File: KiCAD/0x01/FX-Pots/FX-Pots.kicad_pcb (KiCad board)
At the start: 2 copper layers, 50 x 100 mm, 28 parts, among them J1 Conn_01x05, J2 Conn_01x05, SW1 SW_Push_LED, SW2 SW_Push_LED, SW3 SW_Push_LED, SW4 SW_Push_LED, U1 74HC595, U2 CD74HC4067M

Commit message: fx-pots
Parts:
- removed C3: 1uF, Capacitor_SMD:C_1206_3216Metric_Pad1.33x1.80mm_HandSolder
- added C10: 1uF, Capacitor_SMD:C_1206_3216Metric_Pad1.33x1.80mm_HandSolder, F.Cu at (173.7, 105.3)
- added C11: 1uF, Capacitor_SMD:C_1206_3216Metric_Pad1.33x1.80mm_HandSolder, F.Cu at (174.2, 131.7)
- added C5: 1uF, Capacitor_SMD:C_1206_3216Metric_Pad1.33x1.80mm_HandSolder, F.Cu at (86.3, 75.7)
- added C6: 1uF, Capacitor_SMD:C_1206_3216Metric_Pad1.33x1.80mm_HandSolder, F.Cu at (86.1, 104.7)
- added C7: 1uF, Capacitor_SMD:C_1206_3216Metric_Pad1.33x1.80mm_HandSolder, F.Cu at (86.4, 131.5)
- added C8: 1uF, Capacitor_SMD:C_1206_3216Metric_Pad1.33x1.80mm_HandSolder, F.Cu at (174.0, 46.4)
- added C9: 1uF, Capacitor_SMD:C_1206_3216Metric_Pad1.33x1.80mm_HandSolder, F.Cu at (174.2, 76.2)
- added JP1: A0, Jumper:SolderJumper-2_P1.3mm_Open_RoundedPad1.0x1.5mm, B.Cu at (124.2, 90.6)
- added JP2: A1, Jumper:SolderJumper-2_P1.3mm_Open_RoundedPad1.0x1.5mm, B.Cu at (127.8, 90.6)
- added JP3: A0, Jumper:SolderJumper-2_P1.3mm_Open_RoundedPad1.0x1.5mm, B.Cu at (131.3, 90.6)
- added JP4: A1, Jumper:SolderJumper-2_P1.3mm_Open_RoundedPad1.0x1.5mm, B.Cu at (134.9, 90.6)
- added R10: 10K, PCM_Resistor_SMD_AKL:R_1206_3216Metric_Pad1.30x1.75mm_HandSolder, B.Cu at (100.4, 132.4)
- added R11: 220, PCM_Resistor_SMD_AKL:R_1206_3216Metric_Pad1.30x1.75mm_HandSolder, F.Cu at (160.5, 44.2)
- added R12: 220, PCM_Resistor_SMD_AKL:R_1206_3216Metric_Pad1.30x1.75mm_HandSolder, F.Cu at (165.4, 68.1)
- added R13: 220, PCM_Resistor_SMD_AKL:R_1206_3216Metric_Pad1.30x1.75mm_HandSolder, F.Cu at (165.2, 97.7)
- added R14: 220, PCM_Resistor_SMD_AKL:R_1206_3216Metric_Pad1.30x1.75mm_HandSolder, F.Cu at (165.4, 125.2)
- added R15: 10K, PCM_Resistor_SMD_AKL:R_1206_3216Metric_Pad1.30x1.75mm_HandSolder, B.Cu at (174.3, 50.3)
- added R16: 10K, PCM_Resistor_SMD_AKL:R_1206_3216Metric_Pad1.30x1.75mm_HandSolder, B.Cu at (174.1, 79.4)
- added R17: 10K, PCM_Resistor_SMD_AKL:R_1206_3216Metric_Pad1.30x1.75mm_HandSolder, B.Cu at (173.7, 108.5)
- added R18: 10K, PCM_Resistor_SMD_AKL:R_1206_3216Metric_Pad1.30x1.75mm_HandSolder, B.Cu at (174.2, 131.8)
- added R9: 10K, PCM_Resistor_SMD_AKL:R_1206_3216Metric_Pad1.30x1.75mm_HandSolder, F.Cu at (90.4, 112.3)
- added RN1: R_Pack04_10K, Resistor_SMD:R_Array_Convex_4x0603, F.Cu at (129.6, 96.6)
- added RV5: R_Pot, led-switch:Potentiometer_Bourns_PTV09A-1_Single_Vertical, F.Cu at (144.5, 53.6)
- added RV6: R_Pot, led-switch:Potentiometer_Bourns_PTV09A-1_Single_Vertical, F.Cu at (144.6, 82.7)
- added RV7: R_Pot, led-switch:Potentiometer_Bourns_PTV09A-1_Single_Vertical, F.Cu at (144.6, 111.7)
- added RV8: R_Pot, led-switch:Potentiometer_Bourns_PTV09A-1_Single_Vertical, F.Cu at (144.8, 138.2)
- added SW5: SW_Push_LED, led-switch:SW_PUSH_6mm_LED, F.Cu at (167.2, 46.4)
- added SW6: SW_Push_LED, led-switch:SW_PUSH_6mm_LED, F.Cu at (167.5, 75.5)
- added SW7: SW_Push_LED, led-switch:SW_PUSH_6mm_LED, F.Cu at (167.0, 104.6)
- added SW8: SW_Push_LED, led-switch:SW_PUSH_6mm_LED, F.Cu at (167.3, 131.2)
- C1, C2: value 1uF -> 10uF; footprint Capacitor_SMD:C_1206_3216Metric_Pad1.33x1.80mm_HandSolder -> Capacitor_SMD:C_0805_2012Metric_Pad1.18x1.45mm_HandSolder
- C4: moved to F.Cu
- J1: value Conn_01x05 -> IN; footprint Connector_PinSocket_2.54mm:PinSocket_1x05_P2.54mm_Vertical -> Connector_JST:JST_PH_S4B-PH-K_1x04_P2.00mm_Horizontal; moved to B.Cu
- J2: value Conn_01x05 -> OUT; footprint Connector_PinSocket_2.54mm:PinSocket_1x05_P2.54mm_Vertical -> Connector_JST:JST_PH_S4B-PH-K_1x04_P2.00mm_Horizontal; moved to B.Cu
- R1, R2: value 220 -> 10K; footprint PCM_Resistor_SMD_AKL:R_1206_3216Metric_Pad1.30x1.75mm_HandSolder -> Capacitor_SMD:C_0805_2012Metric_Pad1.18x1.45mm_HandSolder
- R5, R6: value 10K -> 220
- RV1, RV2, RV3, RV4: footprint Potentiometer_THT:Potentiometer_Bourns_PTV09A-1_Single_Vertical -> led-switch:Potentiometer_Bourns_PTV09A-1_Single_Vertical
- U1: value 74HC595 -> ADS7830; footprint Package_SO:SOIC-16_3.9x9.9mm_P1.27mm -> Package_SO:TSSOP-16_4.4x5mm_P0.65mm; moved to F.Cu
- U2: value CD74HC4067M -> ADS7830; footprint Package_SO:SOIC-24W_7.5x15.4mm_P1.27mm -> Package_SO:TSSOP-16_4.4x5mm_P0.65mm; moved to F.Cu
- moved C4 93.4 mm to (99.9, 46.8)
- moved J2 86.2 mm to (159.3, 115.5), turned to 180 degrees
- moved C2 78.7 mm to (152.6, 84.2)
- moved R3 65.1 mm to (99.9, 43.6)
- moved J1 63.8 mm to (102.4, 63.0), turned to 0 degrees
- moved R8 63.5 mm to (87.4, 69.1)
- moved R7 62.5 mm to (88.3, 52.7)
- moved H2 62.2 mm to (170.0, 60.7)
- moved H3 62.2 mm to (170.0, 119.6)
- moved U2 49.2 mm to (154.9, 90.7), turned to 90 degrees
- moved C1 44.0 mm to (104.0, 83.7)
- moved R5 41.1 mm to (91.4, 97.8), turned to 0 degrees
- moved R1 27.0 mm to (108.6, 67.3), turned to 90 degrees
- moved U1 25.4 mm to (106.3, 90.8), turned to 90 degrees
- moved R2 24.2 mm to (106.4, 67.3), turned to 90 degrees
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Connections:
- C1 pad 1: FXSW1 -> +5V
- C2 pad 1: FXSW2 -> +5V
- C4 pad 1: FXSW4 -> /FXSW1
- J1 pad 1: MPLEX-S0 -> GND
- J1 pad 2: MPLEX-S1 -> +5V
- J1 pad 3: MPLEX-AP -> /SDA
- J1 pad 4: MPLEX-S2 -> /SCL
- J2 pad 1: GND -> /SCL
- J2 pad 2: +5V -> /SDA
- J2 pad 3: SRCLK -> +5V
- J2 pad 4: FX-LED-LATCH -> GND
- R1 pad 1: GND -> +5V
- R1 pad 2: Net-(SW1-K) -> /SDA
- R2 pad 1: GND -> +5V
- R2 pad 2: Net-(SW2-K) -> /SCL
- R3 pad 2: Net-(SW3-K) -> Net-(SW1-K)
- R4 pad 2: Net-(SW4-K) -> Net-(SW2-K)
- R5 pad 1: +5V -> GND
- R5 pad 2: FXSW1 -> Net-(SW3-K)
- R6 pad 1: +5V -> GND
- R6 pad 2: FXSW2 -> Net-(SW4-K)
- R7 pad 2: FXSW3 -> /FXSW1
- R8 pad 2: FXSW4 -> /FXSW2
- RV1 pad 2: POT1 -> /POT1
- RV2 pad 2: POT2 -> /POT2
- RV3 pad 2: POT3 -> /POT3
- RV4 pad 2: POT4 -> /POT4
- SW1 pad 2: FXSW1 -> /FXSW1
- SW1 pad 4: FX-LED-1 -> /FX-LED-1
- SW2 pad 2: FXSW2 -> /FXSW2
- SW2 pad 4: FX-LED-2 -> /FX-LED-2
- SW3 pad 2: FXSW3 -> /FXSW3
- SW3 pad 4: FX-LED-3 -> /FX-LED-3
- SW4 pad 2: FXSW4 -> /FXSW4
- SW4 pad 4: FX-LED-4 -> /FX-LED-4
- U1 pad 1: unconnected-(U1-QB-Pad1) -> /POT1
- U1 pad 10: +5V -> unconnected-(U1-REFin/REFout-Pad10)
- U1 pad 11: SRCLK -> unconnected-(U1-COM-Pad11)
- U1 pad 12: FX-LED-LATCH -> /A0
- U1 pad 13: GND -> /A1
- U1 pad 14: FX-LED-SIG -> /SCL
- U1 pad 15: unconnected-(U1-QA-Pad15) -> /SDA
- U1 pad 2: FX-LED-1 -> /FXSW1
- U1 pad 3: FX-LED-2 -> /POT2
- U1 pad 4: FX-LED-3 -> /FXSW2
- U1 pad 5: FX-LED-4 -> /POT3
- U1 pad 6: unconnected-(U1-QG-Pad6) -> /FXSW3
- U1 pad 7: unconnected-(U1-QH-Pad7) -> /POT4
- U1 pad 8: GND -> /FXSW4
- U1 pad 9: unconnected-(U1-QH'-Pad9) -> GND
- U2 pad 1: MPLEX-AP -> /POT5
- U2 pad 10: MPLEX-S0 -> unconnected-(U2-REFin/REFout-Pad10)
- U2 pad 11: MPLEX-S1 -> unconnected-(U2-COM-Pad11)
- U2 pad 12: GND -> /A3
- U2 pad 13: MPLEX-S3 -> /A4
- U2 pad 14: MPLEX-S2 -> /SCL
- U2 pad 15: GND -> /SDA
- U2 pad 16: unconnected-(U2-I15-Pad16) -> +5V
- U2 pad 2: unconnected-(U2-I7-Pad2) -> /FXSW5
- U2 pad 3: unconnected-(U2-I6-Pad3) -> /POT6
- U2 pad 4: unconnected-(U2-I5-Pad4) -> /FXSW6
- U2 pad 5: FXSW2 -> /POT7
- U2 pad 6: FXSW1 -> /FXSW7
- U2 pad 7: POT1 -> /POT8
- U2 pad 8: POT2 -> /FXSW8
- U2 pad 9: unconnected-(U2-I0-Pad9) -> GND
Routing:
- added copper zone on B.Cu, net +5V
- added copper zone on F.Cu, net +5V
- added copper zone on F.Cu, net GND
- removed copper zone on B.Cu, net GND
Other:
- board size 50 x 100 mm -> 100.1 x 100 mm

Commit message: pads_demo
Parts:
- moved R1 2.18 mm to (106.4, 67.3)
- moved R2 2.18 mm to (108.6, 67.3)
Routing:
- net /SCL: track 0.00 -> 141.3 mm, vias 0 -> 10
- net /SDA: track 0.00 -> 130.3 mm, vias 0 -> 9
- net GND: track 0.00 -> 99.5 mm, vias 0 -> 1
- net /FXSW5: track 0.00 -> 77.8 mm, vias 0 -> 4
- net /POT8: track 0.00 -> 51.5 mm, vias 0 -> 2
- net /POT5: track 0.00 -> 48.1 mm, vias 0 -> 2
- net /FXSW6: track 0.00 -> 31.6 mm
- net /POT7: track 0.00 -> 30.2 mm
- net /A3: track 0.00 -> 27.5 mm, vias 0 -> 1
- net /A1: track 0.00 -> 26.8 mm, vias 0 -> 1
- net /POT6: track 0.00 -> 22.7 mm, vias 0 -> 1
- net /FXSW7: track 0.00 -> 21.3 mm, vias 0 -> 2
- net /A4: track 0.00 -> 21.0 mm, vias 0 -> 1
- net /A0: track 0.00 -> 18.8 mm, vias 0 -> 1
- net +5V: track 0.00 -> 16.7 mm, vias 0 -> 2
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
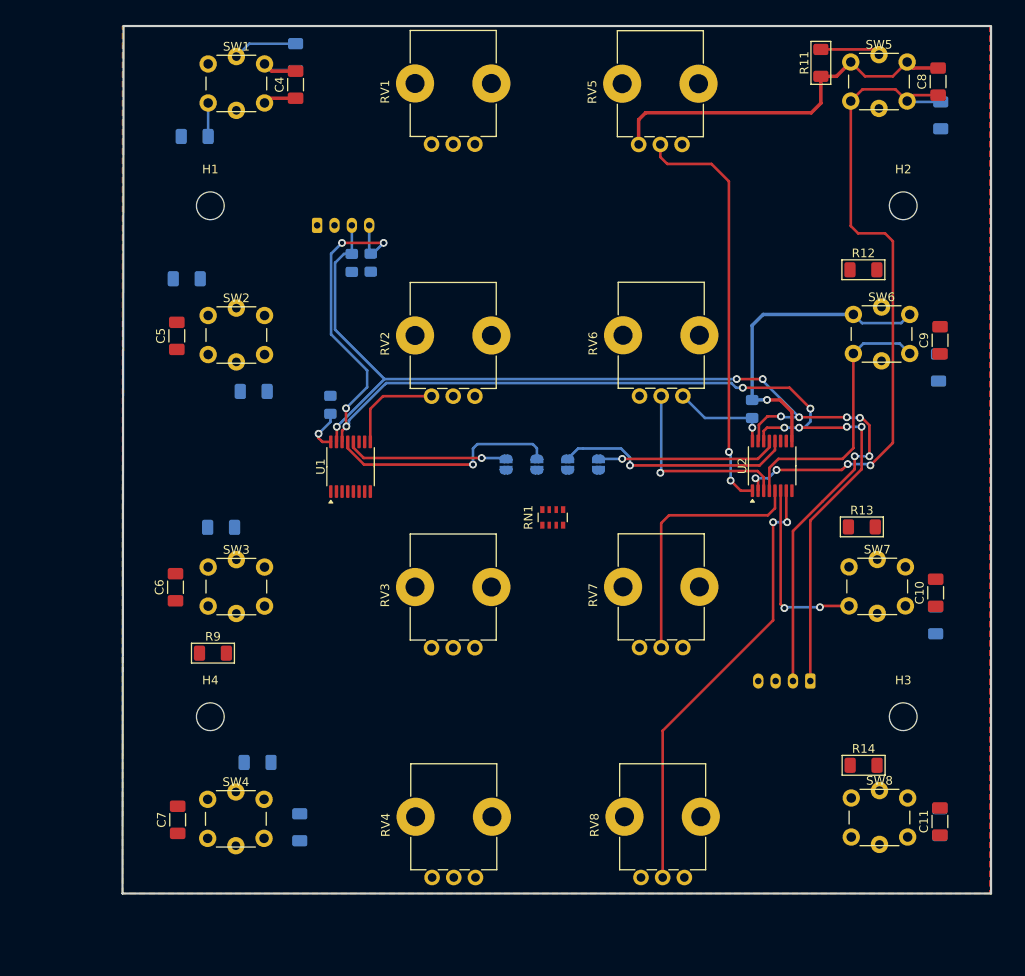
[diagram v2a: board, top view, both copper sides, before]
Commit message: fx pots routing
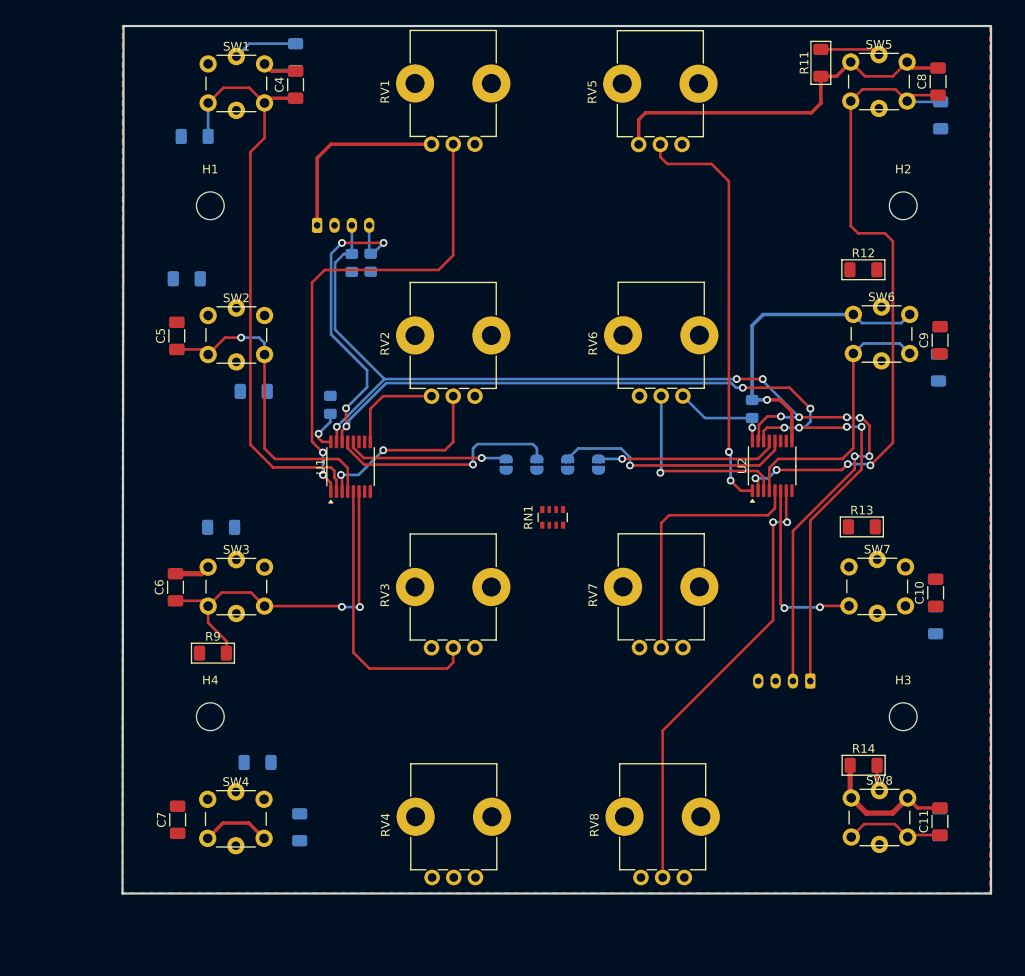
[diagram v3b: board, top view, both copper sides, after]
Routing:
- net /FXSW1: track 7.67 -> 69.1 mm
- net /POT1: track 0.00 -> 55.4 mm, vias 0 -> 2
- net /FXSW3: track 0.00 -> 42.5 mm, vias 0 -> 2
- net GND: track 99.5 -> 141.2 mm
- net /FXSW2: track 0.00 -> 36.8 mm, vias 0 -> 1
- net /POT3: track 0.00 -> 32.8 mm
- net /POT2: track 0.00 -> 21.8 mm, vias 0 -> 2
- net /FXSW8: track 0.00 -> 11.5 mm
- net /FXSW4: track 0.00 -> 7.96 mm
- net Net-(SW8-K): track 0.00 -> 3.04 mm

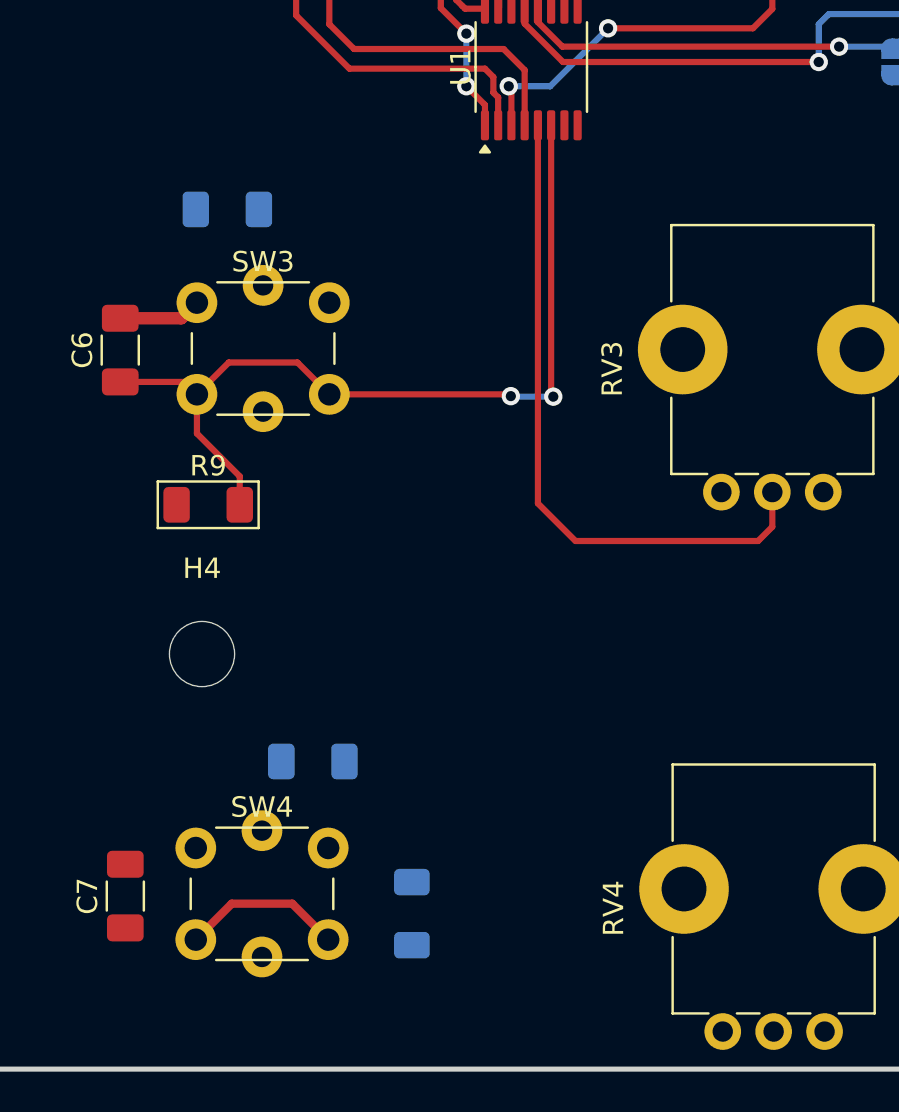
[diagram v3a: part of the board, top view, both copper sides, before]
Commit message: routing fx pots
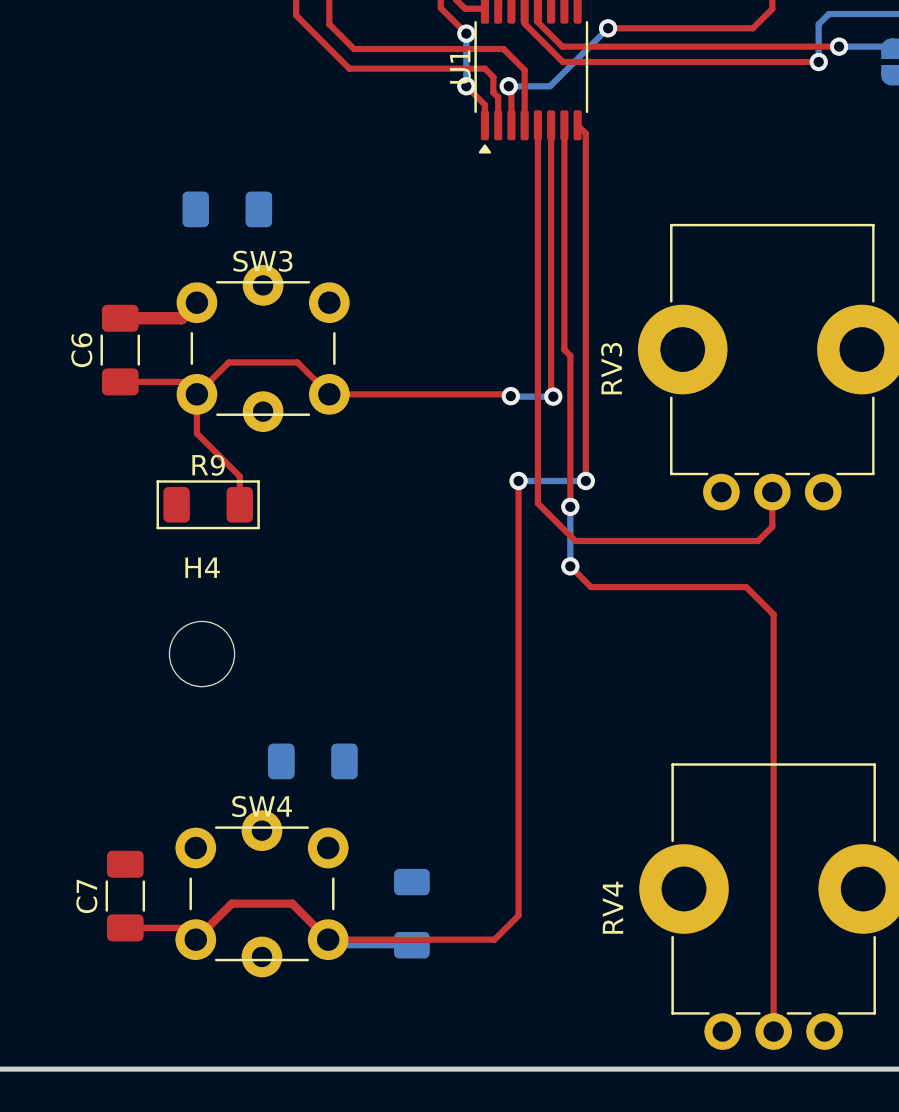
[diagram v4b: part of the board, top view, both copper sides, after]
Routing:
- net /FXSW4: track 7.96 -> 68.0 mm, vias 0 -> 2
- net /POT4: track 0.00 -> 53.2 mm, vias 0 -> 2
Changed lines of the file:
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@@
+	)
+	(segment
+		(start 108.5625 93.6625)
+		(end 108.966 94.066)
+		(width 0.3048)
+		(layer "F.Cu")
+		(net 6)
+	)
+	(segment
+		(start 105.664 132.461)
+		(end 105.664 111.125)
+		(width 0.3048)
+		(layer "F.Cu")
+		(net 6)
+	)
+	(segment
+		(start 96.3156 133.6442)
+		(end 104.4808 133.6442)
+		(width 0.3048)
+		(layer "F.Cu")
+		(net 6)
 	)
 	(segment
@@
 	)
 	(segment
+		(start 89.23778 133.06638)
+		(end 89.8156 133.6442)
+		(width 0.3048)
+		(layer "F.Cu")
+		(net 6)
+	)
+	(segment
 		(start 94.5482 131.8768)
 		(end 96.3156 133.6442)
@@
 	)
 	(segment
+		(start 86.355079 133.06638)
+		(end 89.23778 133.06638)
+		(width 0.3048)
+		(layer "F.Cu")
+		(net 6)
+	)
+	(segment
+		(start 108.966 94.066)
+		(end 108.966 111.125)
+		(width 0.3048)
+		(layer "F.Cu")
+		(net 6)
+	)
+	(segment
+		(start 104.4808 133.6442)
+		(end 105.664 132.461)
+		(width 0.3048)
+		(layer "F.Cu")
+		(net 6)
+	)
+	(segment
 		(start 89.8156 133.6442)
 		(end 91.583 131.8768)
@@
 		(net 6)
 	)
+	(via
+		(at 108.966 111.125)
+		(size 0.9)
+		(drill 0.5)
+		(layers "F.Cu" "B.Cu")
+		(net 6)
+	)
+	(via
+		(at 105.664 111.125)
+		(size 0.9)
+		(drill 0.5)
+		(layers "F.Cu" "B.Cu")
+		(net 6)
+	)
+	(segment
+		(start 108.966 111.125)
+		(end 105.664 111.125)
+		(width 0.3048)
+		(layer "B.Cu")
+		(net 6)
+	)
+	(segment
+		(start 96.58888 133.91748)
+		(end 96.3156 133.6442)
+		(width 0.3048)
+		(layer "B.Cu")
+		(net 6)
+	)
+	(segment
+		(start 100.426679 133.91748)
+		(end 96.58888 133.91748)
+		(width 0.3048)
+		(layer "B.Cu")
+		(net 6)
+	)
 	(segment
 		(start 167.9 63.9)
@@
 	)
 	(segment
+		(start 109.22 116.332)
+		(end 116.84 116.332)
+		(width 0.3048)
+		(layer "F.Cu")
+		(net 32)
+	)
+	(segment
+		(start 108.204 115.316)
+		(end 109.22 116.332)
+		(width 0.3048)
+		(layer "F.Cu")
+		(net 32)
+	)
+	(segment
+		(start 107.9125 93.6625)
+		(end 107.9125 104.683137)
+		(width 0.3048)
+		(layer "F.Cu")
+		(net 32)
+	)
+	(segment
+		(start 108.204 104.974637)
+		(end 108.204 112.395)
+		(width 0.3048)
+		(layer "F.Cu")
+		(net 32)
+	)
+	(segment
+		(start 107.9125 104.683137)
+		(end 108.204 104.974637)
+		(width 0.3048)
+		(layer "F.Cu")
+		(net 32)
+	)
+	(segment
+		(start 118.1862 117.6782)
+		(end 118.1862 138.1554)
+		(width 0.3048)
+		(layer "F.Cu")
+		(net 32)
+	)
+	(segment
+		(start 116.84 116.332)
+		(end 118.1862 117.6782)
+		(width 0.3048)
+		(layer "F.Cu")
+		(net 32)
+	)
+	(via
+		(at 108.204 115.316)
+		(size 0.9)
+		(drill 0.5)
+		(layers "F.Cu" "B.Cu")
+		(net 32)
+	)
+	(via
+		(at 108.204 112.395)
+		(size 0.9)
+		(drill 0.5)
+		(layers "F.Cu" "B.Cu")
+		(net 32)
+	)
+	(segment
+		(start 108.204 112.395)
+		(end 108.204 115.316)
+		(width 0.3048)
+		(layer "B.Cu")
+		(net 32)
+	)
+	(segment

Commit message: fxpots
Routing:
- net GND: track 141.2 -> 529.7 mm, vias 1 -> 12
- net Net-(SW2-K): track 0.00 -> 53.2 mm
- net Net-(SW4-K): track 0.00 -> 47.7 mm
- net /FXSW8: track 11.5 -> 58.7 mm, vias 0 -> 1
- net /SCL: track 141.3 -> 109.9 mm, vias 10 -> 2
- net /SDA: track 130.3 -> 105.7 mm, vias 9 -> 2
- net /FXSW5: track 77.8 -> 64.3 mm, vias 4 -> 1
- net +5V: track 16.7 -> 3.25 mm, vias 2 -> 1
- net /FXSW2: track 36.8 -> 45.9 mm, vias 1 -> 0
- net /FXSW7: track 21.3 -> 30.3 mm, vias 2 -> 0
- net Net-(JP4-B): track 0.00 -> 7.92 mm, vias 0 -> 1
- net /POT1: track 55.4 -> 47.8 mm, vias 2 -> 1
- net Net-(JP1-B): track 0.00 -> 7.48 mm, vias 0 -> 1
- net /FXSW4: track 68.0 -> 61.0 mm, vias 2 -> 1
- net /FXSW3: track 42.5 -> 35.9 mm, vias 2 -> 0
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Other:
- board size 100.1 x 100 mm -> 100 x 100 mm
